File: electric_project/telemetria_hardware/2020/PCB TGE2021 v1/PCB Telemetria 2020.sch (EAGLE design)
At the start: 12 parts, among them IC1 INA240A1DR, IC2 MCP3221A6T-E_OTVAO

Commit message: Begining of 3V3 Regulator Circuit
LDO AZ111 added to the circuit. The input filter is under research.
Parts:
- added 12V_POWER: 43650-0200, 43650-0200:43650-0200
- added C6: 100nF, rcl:C-USC0805
- added IC3: AZ1117IH-3.3TRG1, AZ1117IH-3.3TRG1:AZ1117IH-3.3TRG1
- added U$2: DC-DC-STEP-DOWN-LM2596, diy-modules:DC-DC-STEP-DOWN-LM2596
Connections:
- new net VCC_12V: 12V_POWER.2, U$2.IN+
- new net VCC_5V: IC3.INPUT, U$2.OUT+
- net GND: now also 12V_POWER.1, C6.2, IC3.ADJ/GND, U$2.IN-, U$2.OUT-
- net VCC_3V3: now also C6.1, IC3.OUTPUT, IC3.VOUT
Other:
- note added: "12V INPUT AND CONVERSION"
- note added: "3.3 V Regulator (LDO)"
- note added: "DC/DC 12-05 V BUCK MODULE"
- note added: "POWER 12V CONNECTOR"
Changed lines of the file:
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@@
 <layer number="97" name="Info" color="7" fill="1" visible="yes" active="yes"/>
 <layer number="98" name="Guide" color="6" fill="1" visible="yes" active="yes"/>
+<layer number="101" name="Hidden" color="15" fill="1" visible="yes" active="yes"/>
+<layer number="102" name="Changes" color="12" fill="1" visible="yes" active="yes"/>
 </layers>
 <schematic xreflabel="%F%N/%S.%C%R" xrefpart="/%S.%C%R">
@@
 <part name="C5" library="rcl" library_urn="urn:adsk.eagle:library:334" deviceset="C-US" device="C0805" package3d_urn="urn:adsk.eagle:package:23617/2" value="100nF"/>
 <part name="GND3" library="supply1" library_urn="urn:adsk.eagle:library:371" deviceset="GND" device=""/>
+<part name="FRAME3" library="frames" library_urn="urn:adsk.eagle:library:229" deviceset="A3L-LOC" device=""/>
+<part name="U$2" library="diy-modules" deviceset="DC-DC-STEP-DOWN-LM2596" device=""/>
+<part name="12V_POWER" library="43650-0200" deviceset="43650-0200" device=""/>
+<part name="IC3" library="AZ1117IH-3.3TRG1" deviceset="AZ1117IH-3.3TRG1" device=""/>
+<part name="C6" library="rcl" library_urn="urn:adsk.eagle:library:334" deviceset="C-US" device="C0805" package3d_urn="urn:adsk.eagle:package:23617/2" value="100nF"/>
+<part name="GND4" library="supply1" library_urn="urn:adsk.eagle:library:371" deviceset="GND" device=""/>
 </parts>
 <sheets>
@@
 <description>Power</description>
 <plain>
+<wire x1="45.72" y1="231.14" x2="45.72" y2="187.96" width="0.3048" layer="94"/>
+<wire x1="45.72" y1="187.96" x2="137.16" y2="187.96" width="0.3048" layer="94"/>
+<wire x1="137.16" y1="187.96" x2="137.16" y2="231.14" width="0.3048" layer="94"/>
+<wire x1="137.16" y1="231.14" x2="45.72" y2="231.14" width="0.3048" layer="94"/>
+<text x="76.2" y="226.06" size="1.778" layer="94">DC/DC 12-05 V BUCK MODULE</text>
+<wire x1="12.7" y1="231.14" x2="12.7" y2="187.96" width="0.3048" layer="94"/>
+<wire x1="12.7" y1="187.96" x2="40.64" y2="187.96" width="0.3048" layer="94"/>
+<wire x1="40.64" y1="187.96" x2="40.64" y2="231.14" width="0.3048" layer="94"/>
+<wire x1="40.64" y1="231.14" x2="12.7" y2="231.14" width="0.3048" layer="94"/>
+<text x="20.32" y="223.52" size="1.778" layer="94">POWER 12V
+CONNECTOR</text>
+<wire x1="7.62" y1="248.92" x2="7.62" y2="182.88" width="0.3048" layer="94"/>
+<wire x1="7.62" y1="182.88" x2="142.24" y2="182.88" width="0.3048" layer="94"/>
+<wire x1="142.24" y1="182.88" x2="142.24" y2="248.92" width="0.3048" layer="94"/>
+<wire x1="142.24" y1="248.92" x2="7.62" y2="248.92" width="0.3048" layer="94"/>
+<text x="50.8" y="238.76" size="2.54" layer="94">12V INPUT AND CONVERSION</text>
+<wire x1="149.86" y1="248.92" x2="149.86" y2="182.88" width="0.3048" layer="94"/>
+<wire x1="149.86" y1="182.88" x2="276.86" y2="182.88" width="0.3048" layer="94"/>
+<wire x1="276.86" y1="182.88" x2="276.86" y2="248.92" width="0.3048" layer="94"/>
+<wire x1="276.86" y1="248.92" x2="149.86" y2="248.92" width="0.3048" layer="94"/>
+<wire x1="210.82" y1="228.6" x2="210.82" y2="185.42" width="0.3048" layer="94"/>
+<wire x1="210.82" y1="185.42" x2="274.32" y2="185.42" width="0.3048" layer="94"/>
+<wire x1="274.32" y1="185.42" x2="274.32" y2="228.6" width="0.3048" layer="94"/>
+<wire x1="274.32" y1="228.6" x2="210.82" y2="228.6" width="0.3048" layer="94"/>
+<text x="231.14" y="220.98" size="1.778" layer="94">3.3 V Regulator (LDO)</text>
 </plain>
 <instances>
+<instance part="FRAME3" gate="G$1" x="0" y="0" smashed="yes">
+<attribute name="DRAWING_NAME" x="344.17" y="15.24" size="2.54" layer="94"/>
+<attribute name="LAST_DATE_TIME" x="344.17" y="10.16" size="2.286" layer="94"/>
+<attribute name="SHEET" x="357.505" y="5.08" size="2.54" layer="94"/>
+</instance>
+<instance part="U$2" gate="G$1" x="91.44" y="203.2" smashed="yes">
+<attribute name="NAME" x="78.74" y="218.44" size="1.778" layer="95"/>
+<attribute name="VALUE" x="78.74" y="215.9" size="1.778" layer="96"/>
+</instance>
+<instance part="12V_POWER" gate="G$1" x="25.4" y="203.2" smashed="yes" rot="R90">
+<attribute name="NAME" x="17.78" y="209.55" size="1.778" layer="95" rot="R90" align="center-left"/>
+<attribute name="VALUE" x="20.32" y="209.55" size="1.778" layer="96" rot="R90" align="center-left"/>
+</instance>
+<instance part="IC3" gate="G$1" x="228.6" y="208.28" smashed="yes">
+<attribute name="NAME" x="234.95" y="215.9" size="1.778" layer="95" align="center-left"/>
+<attribute name="VALUE" x="234.95" y="213.36" size="1.778" layer="96" align="center-left"/>
+</instance>
+<instance part="C6" gate="G$1" x="264.16" y="203.2" smashed="yes">
+<attribute name="NAME" x="265.176" y="203.835" size="1.778" layer="95"/>
+<attribute name="VALUE" x="265.176" y="199.009" size="1.778" layer="96"/>
+</instance>
+<instance part="GND4" gate="1" x="264.16" y="193.04" smashed="yes">
+<attribute name="VALUE" x="261.62" y="190.5" size="1.778" layer="96"/>
+</instance>
 </instances>
 <busses>
 </busses>
 <nets>
+<net name="VCC_12V" class="0">
+<segment>
+<pinref part="U$2" gate="G$1" pin="IN+"/>
+<wire x1="73.66" y1="208.28" x2="68.58" y2="208.28" width="0.1524" layer="91"/>
+<label x="68.58" y="208.28" size="1.27" layer="95" rot="R180" xref="yes"/>
+</segment>
+<segment>
+<wire x1="25.4" y1="203.2" x2="25.4" y2="200.66" width="0.1524" layer="91"/>
+<label x="25.4" y="200.66" size="1.27" layer="95" rot="R270" xref="yes"/>
+<pinref part="12V_POWER" gate="G$1" pin="2"/>
+</segment>
+</net>
+<net name="GND" class="0">
+<segment>
+<pinref part="U$2" gate="G$1" pin="IN-"/>
+<wire x1="73.66" y1="198.12" x2="68.58" y2="198.12" width="0.1524" layer="91"/>
+<label x="68.58" y="198.12" size="1.27" layer="95" rot="R180" xref="yes"/>
+</segment>
+<segment>
+<pinref part="U$2" gate="G$1" pin="OUT-"/>
+<wire x1="109.22" y1="198.12" x2="114.3" y2="198.12" width="0.1524" layer="91"/>
+<label x="114.3" y="198.12" size="1.27" layer="95" xref="yes"/>
+</segment>
+<segment>
+<wire x1="27.94" y1="203.2" x2="27.94" y2="200.66" width="0.1524" layer="91"/>
+<label x="27.94" y="200.66" size="1.27" layer="95" rot="R270" xref="yes"/>
+<pinref part="12V_POWER" gate="G$1" pin="1"/>
+</segment>
+<segment>
+<pinref part="IC3" gate="G$1" pin="ADJ/GND"/>
+<wire x1="228.6" y1="208.28" x2="226.06" y2="208.28" width="0.1524" layer="91"/>
+<label x="226.06" y="208.28" size="1.27" layer="95" rot="R180" xref="yes"/>
+</segment>
+<segment>
+<pinref part="GND4" gate="1" pin="GND"/>
+<pinref part="C6" gate="G$1" pin="2"/>
+<wire x1="264.16" y1="195.58" x2="264.16" y2="198.12" width="0.1524" layer="91"/>
+</segment>
+</net>
+<net name="VCC_5V" class="0">
+<segment>
+<pinref part="U$2" gate="G$1" pin="OUT+"/>
+<wire x1="109.22" y1="208.28" x2="114.3" y2="208.28" width="0.1524" layer="91"/>
+<label x="114.3" y="208.28" size="1.27" layer="95" xref="yes"/>
+</segment>
+<segment>
+<pinref part="IC3" gate="G$1" pin="INPUT"/>
+<wire x1="228.6" y1="203.2" x2="226.06" y2="203.2" width="0.1524" layer="91"/>
+<label x="226.06" y="203.2" size="1.27" layer="95" rot="R180" xref="yes"/>
+</segment>
+</net>
+<net name="VCC_3V3" class="0">
+<segment>
+<pinref part="IC3" gate="G$1" pin="VOUT"/>
+<wire x1="261.62" y1="208.28" x2="264.16" y2="208.28" width="0.1524" layer="91"/>
+<label x="266.7" y="210.82" size="1.27" layer="95" rot="R90" xref="yes"/>
+<pinref part="C6" gate="G$1" pin="1"/>
+<wire x1="264.16" y1="205.74" x2="264.16" y2="208.28" width="0.1524" layer="91"/>
+<wire x1="264.16" y1="208.28" x2="266.7" y2="208.28" width="0.1524" layer="91"/>
+<junction x="264.16" y="208.28"/>
+<wire x1="266.7" y1="208.28" x2="266.7" y2="210.82" width="0.1524" layer="91"/>
+</segment>
+<segment>
+<pinref part="IC3" gate="G$1" pin="OUTPUT"/>
+<wire x1="228.6" y1="205.74" x2="226.06" y2="205.74" width="0.1524" layer="91"/>
+<label x="226.06" y="205.74" size="1.27" layer="95" rot="R180" xref="yes"/>
+</segment>
+</net>
 </nets>
 </sheet>

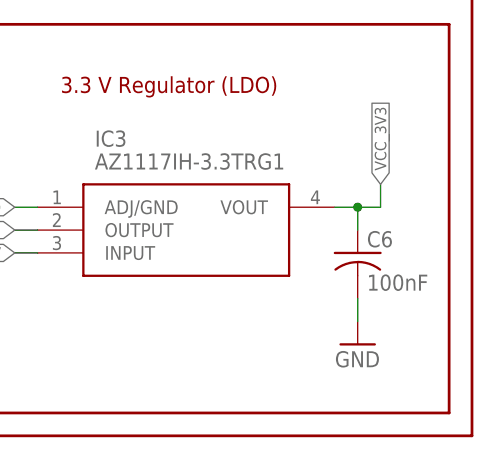
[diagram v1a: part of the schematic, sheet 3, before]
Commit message: apenas corrigi o valor de um capacitor
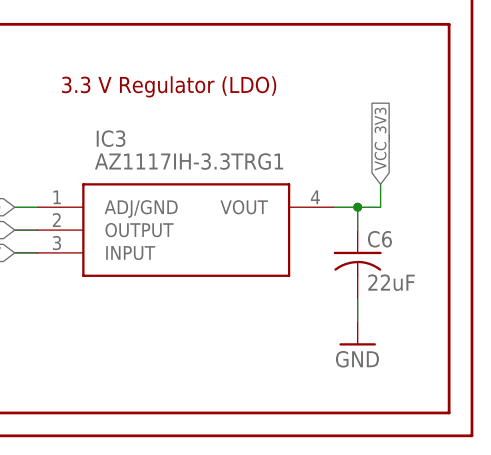
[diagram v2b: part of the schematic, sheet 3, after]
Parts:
- C6: value 100nF -> 22uF
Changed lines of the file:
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@@
 <part name="12V_POWER" library="43650-0200" deviceset="43650-0200" device=""/>
 <part name="IC3" library="AZ1117IH-3.3TRG1" deviceset="AZ1117IH-3.3TRG1" device=""/>
-<part name="C6" library="rcl" library_urn="urn:adsk.eagle:library:334" deviceset="C-US" device="C0805" package3d_urn="urn:adsk.eagle:package:23617/2" value="100nF"/>
+<part name="C6" library="rcl" library_urn="urn:adsk.eagle:library:334" deviceset="C-US" device="C0805" package3d_urn="urn:adsk.eagle:package:23617/2" value="22uF"/>
 <part name="GND4" library="supply1" library_urn="urn:adsk.eagle:library:371" deviceset="GND" device=""/>
 </parts>

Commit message: Ajustes de posicionamento no sch e brd
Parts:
- added C7: 22uF, rcl:C-USC0805
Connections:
- net GND: now also C7.2
- net VCC_5V: now also C7.1
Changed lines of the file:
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@@
 <part name="C6" library="rcl" library_urn="urn:adsk.eagle:library:334" deviceset="C-US" device="C0805" package3d_urn="urn:adsk.eagle:package:23617/2" value="22uF"/>
 <part name="GND4" library="supply1" library_urn="urn:adsk.eagle:library:371" deviceset="GND" device=""/>
+<part name="C7" library="rcl" library_urn="urn:adsk.eagle:library:334" deviceset="C-US" device="C0805" package3d_urn="urn:adsk.eagle:package:23617/2" value="22uF"/>
+<part name="GND5" library="supply1" library_urn="urn:adsk.eagle:library:371" deviceset="GND" device=""/>
 </parts>
 <sheets>
@@
 <wire x1="154.94" y1="154.94" x2="154.94" y2="246.38" width="0.1524" layer="94"/>
 <wire x1="154.94" y1="246.38" x2="12.7" y2="246.38" width="0.1524" layer="94"/>
-<text x="48.26" y="241.3" size="2.54" layer="94">MOTOR SHUNT CURRENT SENSE</text>
+<text x="58.42" y="241.3" size="2.54" layer="94">MOTOR SHUNT CURRENT SENSE</text>
 <wire x1="15.24" y1="233.68" x2="15.24" y2="198.12" width="0.1524" layer="94"/>
 <wire x1="15.24" y1="198.12" x2="106.68" y2="198.12" width="0.1524" layer="94"/>
@@
 <attribute name="VALUE" x="261.62" y="190.5" size="1.778" layer="96"/>
 </instance>
+<instance part="C7" gate="G$1" x="223.52" y="198.12" smashed="yes">
+<attribute name="NAME" x="224.536" y="198.755" size="1.778" layer="95"/>
+<attribute name="VALUE" x="224.536" y="193.929" size="1.778" layer="96"/>
+</instance>
+<instance part="GND5" gate="1" x="223.52" y="187.96" smashed="yes">
+<attribute name="VALUE" x="220.98" y="185.42" size="1.778" layer="96"/>
+</instance>
 </instances>
 <busses>
@@
 <wire x1="264.16" y1="195.58" x2="264.16" y2="198.12" width="0.1524" layer="91"/>
 </segment>
+<segment>
+<pinref part="GND5" gate="1" pin="GND"/>
+<pinref part="C7" gate="G$1" pin="2"/>
+<wire x1="223.52" y1="190.5" x2="223.52" y2="193.04" width="0.1524" layer="91"/>
+</segment>
 </net>
 <net name="VCC_5V" class="0">
@@
 <segment>
 <pinref part="IC3" gate="G$1" pin="INPUT"/>
-<wire x1="228.6" y1="203.2" x2="226.06" y2="203.2" width="0.1524" layer="91"/>
-<label x="226.06" y="203.2" size="1.27" layer="95" rot="R180" xref="yes"/>
-</segment>
-</net>
+<wire x1="228.6" y1="203.2" x2="223.52" y2="203.2" width="0.1524" layer="91"/>
+<label x="220.98" y="203.2" size="1.27" layer="95" rot="R180" xref="yes"/>
+<pinref part="C7" gate="G$1" pin="1"/>
+<wire x1="223.52" y1="203.2" x2="220.98" y2="203.2" width="0.1524" layer="91"/>
+<wire x1="223.52" y1="200.66" x2="223.52" y2="203.2" width="0.1524" layer="91"/>
+<junction x="223.52" y="203.2"/>
+</segment>
+</net>

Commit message: Renaming motor shunt signals
i had named the shunt signals with the sufix _N and _P but this is understood as differential signals on eagle.
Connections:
- net MSHUNT_N renamed MSHUNT_M
- net MSHUNT_P renamed MSHUNT_B
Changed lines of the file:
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@@
 </busses>
 <nets>
-<net name="MSHUNT_N" class="0">
-<segment>
-<pinref part="IC1" gate="G$1" pin="IN-"/>
-<wire x1="50.8" y1="213.36" x2="48.26" y2="213.36" width="0.1524" layer="91"/>
-<label x="48.26" y="213.36" size="1.27" layer="95" rot="R180" xref="yes"/>
-</segment>
-<segment>
-<pinref part="MSHUNT" gate="G$1" pin="2"/>
-<wire x1="134.62" y1="175.26" x2="137.16" y2="175.26" width="0.1524" layer="91"/>
-<label x="137.16" y="175.26" size="1.27" layer="95" xref="yes"/>
-</segment>
-</net>
 <net name="GND" class="0">
 <segment>
@@
 <wire x1="132.08" y1="208.28" x2="132.08" y2="205.74" width="0.1524" layer="91"/>
 <pinref part="GND3" gate="1" pin="GND"/>
-</segment>
-</net>
-<net name="MSHUNT_P" class="0">
-<segment>
-<pinref part="IC1" gate="G$1" pin="IN+"/>
-<wire x1="78.74" y1="213.36" x2="81.28" y2="213.36" width="0.1524" layer="91"/>
-<label x="81.28" y="213.36" size="1.27" layer="95" xref="yes"/>
-</segment>
-<segment>
-<pinref part="MSHUNT" gate="G$1" pin="1"/>
-<wire x1="134.62" y1="172.72" x2="137.16" y2="172.72" width="0.1524" layer="91"/>
-<label x="137.16" y="172.72" size="1.27" layer="95" xref="yes"/>
 </segment>
 </net>
@@
 </segment>
 </net>
+<net name="MSHUNT_M" class="0">
+<segment>
+<pinref part="IC1" gate="G$1" pin="IN-"/>
+<wire x1="50.8" y1="213.36" x2="48.26" y2="213.36" width="0.1524" layer="91"/>
+<label x="48.26" y="213.36" size="1.27" layer="95" rot="R180" xref="yes"/>
+</segment>
+<segment>
+<wire x1="134.62" y1="175.26" x2="137.16" y2="175.26" width="0.1524" layer="91"/>
+<label x="137.16" y="175.26" size="1.27" layer="95" xref="yes"/>
+<pinref part="MSHUNT" gate="G$1" pin="2"/>
+</segment>
+</net>
+<net name="MSHUNT_B" class="0">
+<segment>
+<pinref part="IC1" gate="G$1" pin="IN+"/>
+<wire x1="78.74" y1="213.36" x2="81.28" y2="213.36" width="0.1524" layer="91"/>
+<label x="81.28" y="213.36" size="1.27" layer="95" xref="yes"/>
+</segment>
+<segment>
+<wire x1="134.62" y1="172.72" x2="137.16" y2="172.72" width="0.1524" layer="91"/>
+<label x="137.16" y="172.72" size="1.27" layer="95" xref="yes"/>
+<pinref part="MSHUNT" gate="G$1" pin="1"/>
+</segment>
+</net>

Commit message: Starting ACS758 circuit.
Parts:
- added C8: (no value), rcl:C-USC0805
- added IC4: ACS758LCB-050B-PFF-T, allegro:ACS758LCB-050B-PFF-T
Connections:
- new net MPPT_COUT: IC4.VOUT
- net GND: now also C8.2, IC4.GND
- net VCC_3V3: now also C8.1, IC4.VCC
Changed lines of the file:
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@@
 <part name="GND3" library="supply1" library_urn="urn:adsk.eagle:library:371" deviceset="GND" device=""/>
 <part name="FRAME3" library="frames" library_urn="urn:adsk.eagle:library:229" deviceset="A3L-LOC" device=""/>
-<part name="U$2" library="diy-modules" deviceset="DC-DC-STEP-DOWN-LM2596" device=""/>
+<part name="U$2" library="diy-modules" deviceset="DC-DC-STEP-DOWN-LM2596" device="" override_package3d_urn="urn:adsk.eagle:package:22688648/2" override_package_urn="urn:adsk.eagle:footprint:22688649/1"/>
 <part name="12V_POWER" library="43650-0200" deviceset="43650-0200" device=""/>
 <part name="IC3" library="AZ1117IH-3.3TRG1" deviceset="AZ1117IH-3.3TRG1" device=""/>
@@
 <part name="C7" library="rcl" library_urn="urn:adsk.eagle:library:334" deviceset="C-US" device="C0805" package3d_urn="urn:adsk.eagle:package:23617/2" value="22uF"/>
 <part name="GND5" library="supply1" library_urn="urn:adsk.eagle:library:371" deviceset="GND" device=""/>
+<part name="IC4" library="allegro" library_urn="urn:adsk.eagle:library:93" deviceset="ACS758*" device="" package3d_urn="urn:adsk.eagle:package:3449/1" technology="LCB-050B-PFF-T"/>
+<part name="GND6" library="supply1" library_urn="urn:adsk.eagle:library:371" deviceset="GND" device=""/>
+<part name="C8" library="rcl" library_urn="urn:adsk.eagle:library:334" deviceset="C-US" device="C0805" package3d_urn="urn:adsk.eagle:package:23617/2"/>
+<part name="GND7" library="supply1" library_urn="urn:adsk.eagle:library:371" deviceset="GND" device=""/>
 </parts>
 <sheets>
@@
 <attribute name="VALUE" x="129.54" y="200.66" size="1.778" layer="96"/>
 </instance>
+<instance part="IC4" gate="G$1" x="198.12" y="215.9" smashed="yes" rot="R270">
+<attribute name="NAME" x="207.01" y="218.44" size="1.778" layer="95" rot="R270"/>
+<attribute name="VALUE" x="187.96" y="218.44" size="1.778" layer="96" rot="R270"/>
+</instance>
+<instance part="GND6" gate="1" x="193.04" y="198.12" smashed="yes">
+<attribute name="VALUE" x="190.5" y="195.58" size="1.778" layer="96"/>
+</instance>
+<instance part="C8" gate="G$1" x="172.72" y="210.82" smashed="yes">
+<attribute name="NAME" x="173.736" y="211.455" size="1.778" layer="95"/>
+<attribute name="VALUE" x="173.736" y="206.629" size="1.778" layer="96"/>
+</instance>
+<instance part="GND7" gate="1" x="172.72" y="200.66" smashed="yes">
+<attribute name="VALUE" x="170.18" y="198.12" size="1.778" layer="96"/>
+</instance>
 </instances>
 <busses>
@@
 <wire x1="132.08" y1="208.28" x2="132.08" y2="205.74" width="0.1524" layer="91"/>
 <pinref part="GND3" gate="1" pin="GND"/>
+</segment>
+<segment>
+<pinref part="IC4" gate="G$1" pin="GND"/>
+<pinref part="GND6" gate="1" pin="GND"/>
+<wire x1="193.04" y1="205.74" x2="193.04" y2="200.66" width="0.1524" layer="91"/>
+</segment>
+<segment>
+<pinref part="C8" gate="G$1" pin="2"/>
+<wire x1="172.72" y1="205.74" x2="172.72" y2="203.2" width="0.1524" layer="91"/>
+<pinref part="GND7" gate="1" pin="GND"/>
 </segment>
 </net>
@@
 <label x="81.28" y="185.42" size="1.27" layer="95" rot="R180" xref="yes"/>
 </segment>
+<segment>
+<pinref part="IC4" gate="G$1" pin="VCC"/>
+<label x="203.2" y="198.12" size="1.27" layer="95" xref="yes"/>
+<wire x1="203.2" y1="198.12" x2="203.2" y2="205.74" width="0.1524" layer="91"/>
+</segment>
+<segment>
+<pinref part="C8" gate="G$1" pin="1"/>
+<wire x1="172.72" y1="213.36" x2="172.72" y2="215.9" width="0.1524" layer="91"/>
+<wire x1="172.72" y1="215.9" x2="170.18" y2="215.9" width="0.1524" layer="91"/>
+<label x="170.18" y="215.9" size="1.27" layer="95" rot="R180" xref="yes"/>
+</segment>
 </net>
 <net name="MSHUNT_AMP" class="0">
@@
 <label x="137.16" y="172.72" size="1.27" layer="95" xref="yes"/>
 <pinref part="MSHUNT" gate="G$1" pin="1"/>
+</segment>
+</net>
+<net name="MPPT_COUT" class="0">
+<segment>
+<pinref part="IC4" gate="G$1" pin="VOUT"/>
+<wire x1="198.12" y1="205.74" x2="198.12" y2="200.66" width="0.1524" layer="91"/>
+<label x="198.12" y="200.66" size="1.27" layer="95" rot="R270" xref="yes"/>
 </segment>
 </net>
@@
 packages will not be understood (or retained) with this version.
 </note>
+<note version="9.4" severity="warning">
+Since Version 9.4, EAGLE supports the overriding of 3D packages
+in schematics and board files. Those overridden 3d packages
+will not be understood (or retained) with this version.
+</note>
 <note version="8.4" severity="warning">
